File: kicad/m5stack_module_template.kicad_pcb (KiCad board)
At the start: 2 copper layers, 50 x 50 mm, 332 parts

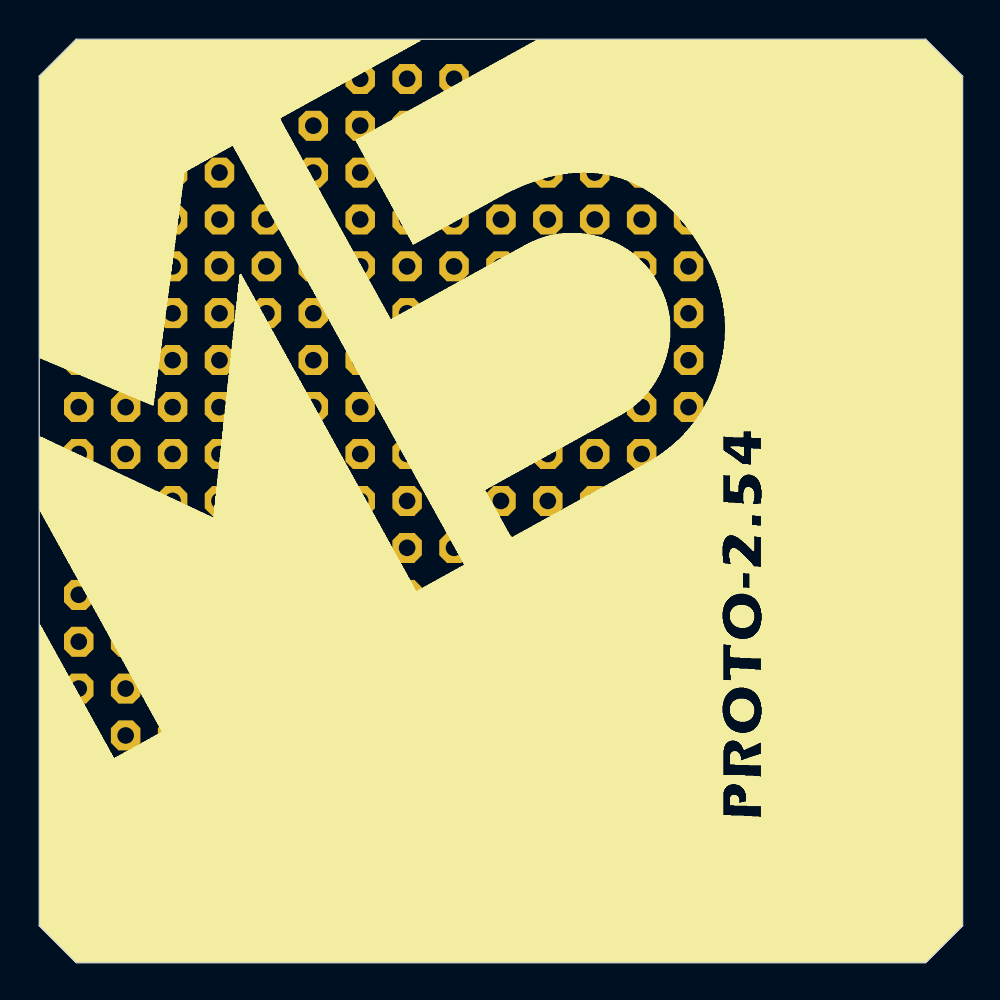
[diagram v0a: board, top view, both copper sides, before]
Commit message: Removed silkscreen and proto pads
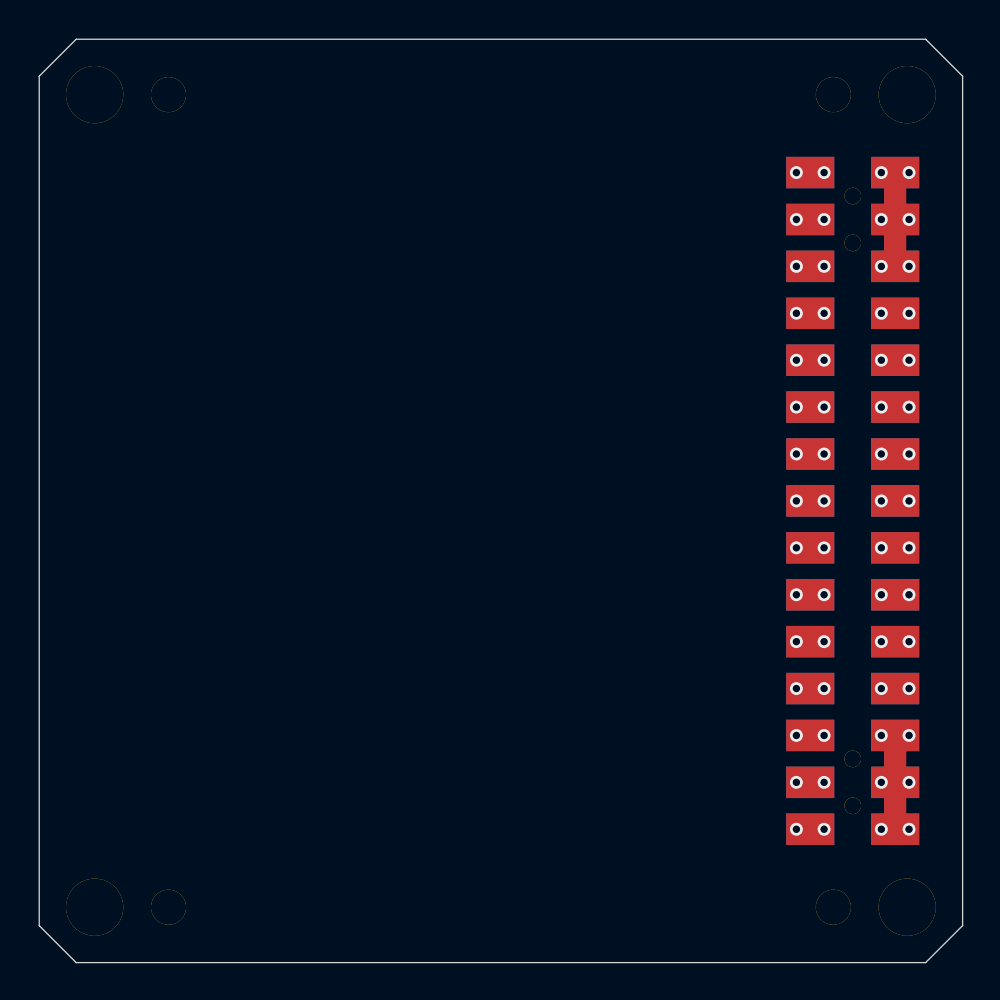
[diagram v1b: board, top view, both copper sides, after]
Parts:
- removed the ? at (26.9, 19.2)
- removed the ? at (49.7, 57.3)
- removed the ? at (37.0, 54.8)
- removed the ? at (34.5, 65.0)
- removed the ? at (34.5, 62.4)
- removed the ? at (34.5, 59.9)
- removed the ? at (34.5, 57.3)
- removed the ? at (34.5, 54.8)
- removed the ? at (31.9, 65.0)
- removed the ? at (31.9, 62.4)
- removed the ? at (31.9, 59.9)
- removed the ? at (31.9, 57.3)
- removed the ? at (52.3, 57.3)
- removed the ? at (31.9, 54.8)
- removed the ? at (29.4, 65.0)
- removed the ? at (29.4, 62.4)
- removed the ? at (29.4, 59.9)
- removed the ? at (29.4, 57.3)
- removed the ? at (29.4, 54.8)
- removed the ? at (26.9, 59.9)
- removed the ? at (26.9, 57.3)
- removed the ? at (26.9, 54.8)
- removed the ? at (26.9, 52.3)
- removed the ? at (52.3, 54.8)
- removed the ? at (26.9, 49.7)
- removed the ? at (26.9, 47.2)
- removed the ? at (26.9, 44.6)
- removed the ? at (26.9, 42.1)
- removed the ? at (24.3, 52.3)
- removed the ? at (24.3, 49.7)
- removed the ? at (24.3, 47.2)
- removed the ? at (24.3, 44.6)
- removed the ? at (24.3, 42.1)
- removed the ? at (21.8, 52.3)
- removed the ? at (37.0, 49.7)
- removed the ? at (21.8, 49.7)
- removed the ? at (21.8, 47.2)
- removed the ? at (21.8, 44.6)
- removed the ? at (21.8, 42.1)
- removed the ? at (19.2, 52.3)
- removed the ? at (19.2, 49.7)
- removed the ? at (19.2, 47.2)
- removed the ? at (19.2, 44.6)
- removed the ? at (19.2, 42.1)
- removed the ? at (19.2, 39.6)
- removed the ? at (37.0, 47.2)
- removed the ? at (21.8, 39.6)
- removed the ? at (24.3, 39.6)
- removed the ? at (26.9, 39.6)
- removed the ? at (19.2, 54.8)
- removed the ? at (21.8, 54.8)
- removed the ? at (24.3, 54.8)
- removed the ? at (19.2, 57.3)
- removed the ? at (21.8, 57.3)
- removed the ? at (24.3, 57.3)
- removed the ? at (19.2, 59.9)
- removed the ? at (37.0, 44.6)
- removed the ? at (21.8, 59.9)
- removed the ? at (24.3, 59.9)
- removed the ? at (47.2, 19.2)
- removed the ? at (49.7, 19.2)
- removed the ? at (52.3, 19.2)
- removed the ? at (39.6, 19.2)
- removed the ? at (42.1, 19.2)
- removed the ? at (44.6, 19.2)
- removed the ? at (31.9, 19.2)
- removed the ? at (34.5, 19.2)
- removed the ? at (37.0, 42.1)
- removed the ? at (37.0, 19.2)
- removed the ? at (47.2, 21.8)
- removed the ? at (49.7, 21.8)
- removed the ? at (52.3, 21.8)
- removed the ? at (39.6, 21.8)
- removed the ? at (42.1, 21.8)
- removed the ? at (44.6, 21.8)
- removed the ? at (31.9, 21.8)
- removed the ? at (34.5, 21.8)
- removed the ? at (37.0, 21.8)
- removed the ? at (37.0, 39.6)
- removed the ? at (29.4, 21.8)
- removed the ? at (29.4, 19.2)
- removed the ? at (29.4, 52.3)
- removed the ? at (31.9, 52.3)
- removed the ? at (34.5, 52.3)
- removed the ? at (37.0, 52.3)
- removed the ? at (29.4, 39.6)
- removed the ? at (29.4, 42.1)
- removed the ? at (29.4, 44.6)
- removed the ? at (29.4, 47.2)
- removed the ? at (34.5, 49.7)
- removed the ? at (29.4, 49.7)
- removed the ? at (49.7, 54.8)
- removed the ? at (29.4, 37.0)
- removed the ? at (26.9, 37.0)
- removed the ? at (24.3, 37.0)
- removed the ? at (21.8, 37.0)
- removed the ? at (19.2, 37.0)
- removed the ? at (47.2, 37.0)
- removed the ? at (44.6, 37.0)
- removed the ? at (42.1, 37.0)
- removed the ? at (34.5, 47.2)
- removed the ? at (39.6, 37.0)
- removed the ? at (31.9, 37.0)
- removed the ? at (34.5, 37.0)
- removed the ? at (37.0, 37.0)
- removed the ? at (37.0, 34.5)
- removed the ? at (34.5, 34.5)
- removed the ? at (31.9, 34.5)
- removed the ? at (39.6, 34.5)
- removed the ? at (42.1, 34.5)
- removed the ? at (44.6, 34.5)
- removed the ? at (34.5, 24.3)
- removed the ? at (34.5, 44.6)
- removed the ? at (47.2, 34.5)
- removed the ? at (19.2, 34.5)
- removed the ? at (21.8, 34.5)
- removed the ? at (24.3, 34.5)
- removed the ? at (26.9, 34.5)
- removed the ? at (29.4, 34.5)
- removed the ? at (49.7, 34.5)
- removed the ? at (52.3, 34.5)
- removed the ? at (37.0, 31.9)
- removed the ? at (34.5, 31.9)
- removed the ? at (34.5, 42.1)
- removed the ? at (31.9, 31.9)
- removed the ? at (39.6, 31.9)
- removed the ? at (42.1, 31.9)
- removed the ? at (44.6, 31.9)
- removed the ? at (47.2, 31.9)
- removed the ? at (19.2, 31.9)
- removed the ? at (21.8, 31.9)
- removed the ? at (24.3, 31.9)
- removed the ? at (26.9, 31.9)
- removed the ? at (29.4, 31.9)
- removed the ? at (34.5, 39.6)
- removed the ? at (49.7, 31.9)
- removed the ? at (52.3, 31.9)
- removed the ? at (37.0, 29.4)
- removed the ? at (34.5, 29.4)
- removed the ? at (31.9, 29.4)
- removed the ? at (39.6, 29.4)
- removed the ? at (42.1, 29.4)
- removed the ? at (44.6, 29.4)
- removed the ? at (47.2, 29.4)
- removed the ? at (19.2, 29.4)
- removed the ? at (31.9, 49.7)
- removed the ? at (21.8, 29.4)
- removed the ? at (24.3, 29.4)
- removed the ? at (26.9, 29.4)
- removed the ? at (29.4, 29.4)
- removed the ? at (49.7, 29.4)
- removed the ? at (52.3, 29.4)
- removed the ? at (37.0, 26.9)
- removed the ? at (34.5, 26.9)
- removed the ? at (31.9, 26.9)
- removed the ? at (39.6, 26.9)
- removed the ? at (31.9, 47.2)
- removed the ? at (42.1, 26.9)
- removed the ? at (44.6, 26.9)
- removed the ? at (47.2, 26.9)
- removed the ? at (19.2, 26.9)
- removed the ? at (21.8, 26.9)
- removed the ? at (24.3, 26.9)
- removed the ? at (26.9, 26.9)
- removed the ? at (29.4, 26.9)
- removed the ? at (49.7, 26.9)
- removed the ? at (52.3, 26.9)
- removed the ? at (31.9, 44.6)
- removed the ? at (37.0, 24.3)
- removed the ? at (31.9, 24.3)
- removed the ? at (39.6, 24.3)
- removed the ? at (42.1, 24.3)
- removed the ? at (44.6, 24.3)
- removed the ? at (47.2, 24.3)
- removed the ? at (19.2, 24.3)
- removed the ? at (21.8, 24.3)
- removed the ? at (24.3, 24.3)
- removed the ? at (26.9, 24.3)
- removed the ? at (31.9, 42.1)
- removed the ? at (29.4, 24.3)
- removed the ? at (49.7, 24.3)
- removed the ? at (52.3, 24.3)
- removed the ? at (49.7, 62.4)
- removed the ? at (52.3, 62.4)
- removed the ? at (49.7, 65.0)
- removed the ? at (52.3, 65.0)
- removed the ? at (54.8, 65.0)
- removed the ? at (54.8, 62.4)
- removed the ? at (54.8, 21.8)
- removed the ? at (31.9, 39.6)
- removed the ? at (57.3, 62.4)
- removed the ? at (57.3, 65.0)
- removed the ? at (57.3, 21.8)
- removed the ? at (52.3, 59.9)
- removed the ? at (42.1, 42.1)
- removed the ? at (49.7, 59.9)
- removed the ? at (44.6, 42.1)
- removed the ? at (47.2, 42.1)
- removed the ? at (49.7, 42.1)
- removed the ? at (52.3, 42.1)
- removed the ? at (39.6, 42.1)
- removed the ? at (39.6, 39.6)
- removed the ? at (42.1, 39.6)
- removed the ? at (44.6, 39.6)
- removed the ? at (47.2, 39.6)
- removed the ? at (52.3, 37.0)
- removed the ? at (49.7, 39.6)
- removed the ? at (52.3, 39.6)
- removed the ? at (52.3, 44.6)
- removed the ? at (49.7, 44.6)
- removed the ? at (47.2, 44.6)
- removed the ? at (44.6, 44.6)
- removed the ? at (42.1, 44.6)
- removed the ? at (39.6, 44.6)
- removed the ? at (39.6, 47.2)
- removed the ? at (52.3, 47.2)
- removed the ? at (49.7, 37.0)
- removed the ? at (49.7, 47.2)
- removed the ? at (47.2, 47.2)
- removed the ? at (44.6, 47.2)
- removed the ? at (42.1, 47.2)
- removed the ? at (52.3, 49.7)
- removed the ? at (49.7, 49.7)
- removed the ? at (47.2, 49.7)
- removed the ? at (44.6, 49.7)
- removed the ? at (42.1, 49.7)
- removed the ? at (39.6, 49.7)
- removed the ? at (26.9, 21.8)
- removed the ? at (39.6, 52.3)
- removed the ? at (52.3, 52.3)
- removed the ? at (49.7, 52.3)
- removed the ? at (47.2, 52.3)
- removed the ? at (44.6, 52.3)
- removed the ? at (42.1, 52.3)
- removed the ? at (47.2, 54.8)
- removed the ? at (44.6, 54.8)
- removed the ? at (42.1, 54.8)
- removed the ? at (39.6, 54.8)
- removed the ? at (26.9, 62.4)
- removed the ? at (39.6, 57.3)
- removed the ? at (47.2, 57.3)
- removed the ? at (44.6, 57.3)
- removed the ? at (42.1, 57.3)
- removed the ? at (47.2, 59.9)
- removed the ? at (44.6, 59.9)
- removed the ? at (42.1, 59.9)
- removed the ? at (39.6, 59.9)
- removed the ? at (39.6, 62.4)
- removed the ? at (47.2, 62.4)
- removed the ? at (26.9, 65.0)
- removed the ? at (44.6, 62.4)
- removed the ? at (42.1, 62.4)
- removed the ? at (42.1, 65.0)
- removed the ? at (44.6, 65.0)
- removed the ? at (47.2, 65.0)
- removed the ? at (39.6, 65.0)
- removed the ? at (37.0, 65.0)
- removed the ? at (37.0, 62.4)
- removed the ? at (37.0, 59.9)
- removed the ? at (37.0, 57.3)

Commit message: Create header footprint
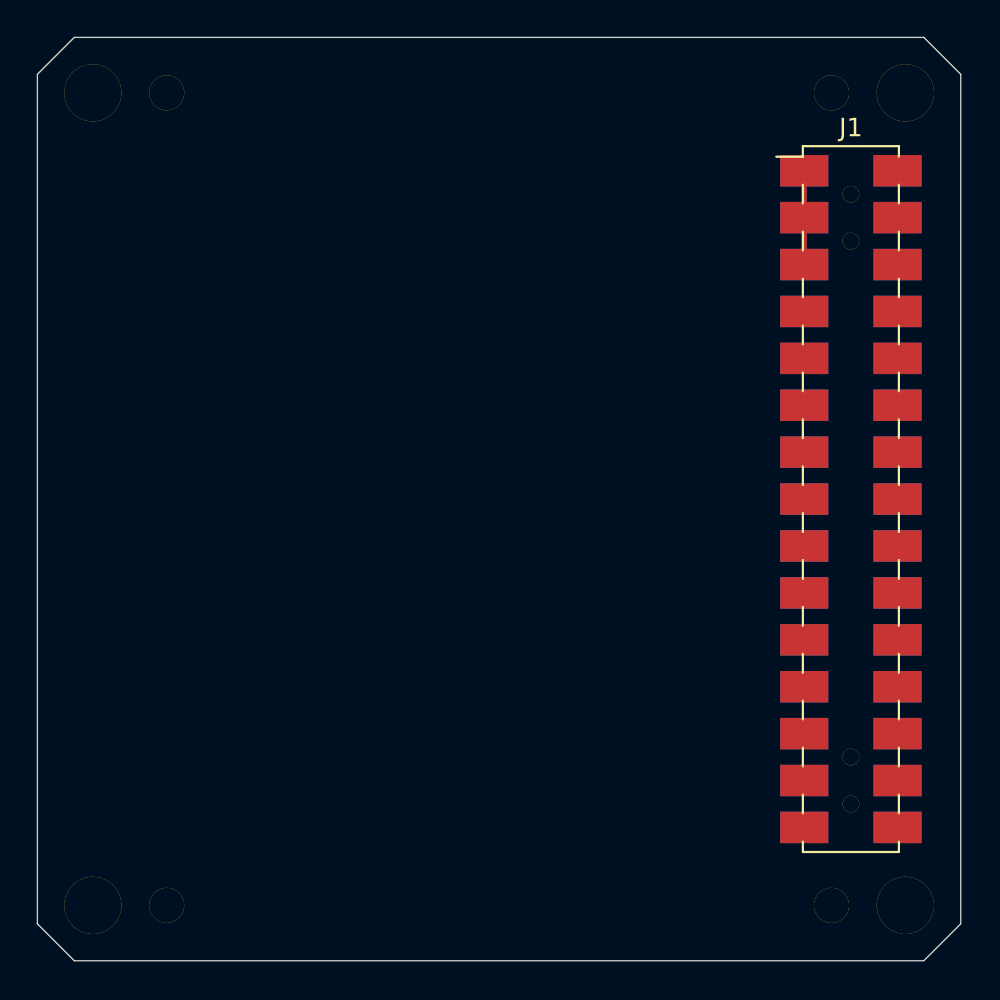
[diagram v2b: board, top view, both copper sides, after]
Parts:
- removed the ? at (58.9, 29.4) (x2)
- removed the ? at (63.5, 29.4) (x2)
- removed the ? at (63.5, 26.9) (x2)
- removed the ? at (58.9, 26.9) (x2)
- removed the ? at (63.5, 24.3) (x2)
- removed the ? at (58.9, 24.3) (x2)
- removed the ? at (58.9, 39.6) (x2)
- removed the ? at (63.5, 39.6) (x2)
- removed the ? at (63.5, 37.0) (x2)
- removed the ? at (58.9, 37.0) (x2)
- removed the ? at (63.5, 34.5) (x2)
- removed the ? at (58.9, 34.5) (x2)
- removed the ? at (63.5, 31.9) (x2)
- removed the ? at (58.9, 31.9) (x2)
- removed the ? at (58.9, 49.7) (x2)
- removed the ? at (63.5, 49.7) (x2)
- removed the ? at (63.5, 47.2) (x2)
- removed the ? at (58.9, 47.2) (x2)
- removed the ? at (63.5, 44.6) (x2)
- removed the ? at (58.9, 44.6) (x2)
- removed the ? at (63.5, 42.1) (x2)
- removed the ? at (58.9, 42.1) (x2)
- removed the ? at (58.9, 52.3) (x2)
- removed the ? at (63.5, 52.3) (x2)
- removed the ? at (58.9, 54.8) (x2)
- removed the ? at (63.5, 54.8) (x2)
- removed the ? at (58.9, 57.3) (x2)
- removed the ? at (63.5, 57.3) (x2)
- removed the ? at (63.5, 59.9) (x2)
- removed the ? at (58.9, 59.9) (x2)
- added J1: Conn_02x15_Odd_Even, M5Stack-Module-Template:M5Stack_PinHeader_2x15_P2.54mm, F.Cu at (61.1, 42.0)
- moved ? 0.14 mm to (64.0, 64.0)
- moved ? 0.14 mm to (20.0, 64.0)
- moved ? 0.14 mm to (64.0, 20.0)
- moved ? 0.14 mm to (24.0, 64.0)
- moved ? 0.14 mm to (61.1, 58.5)
- moved ? 0.14 mm to (61.1, 28.0)
- moved ? 0.14 mm to (61.1, 56.0)
- moved ? 0.14 mm to (20.0, 20.0)
- moved ? 0.14 mm to (24.0, 20.0)
- moved ? 0.14 mm to (60.0, 64.0)
- moved ? 0.14 mm to (61.1, 25.5)
- moved ? 0.14 mm to (60.0, 20.0)
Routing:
- net GND: track 0.00 -> 5.08 mm
- net (no net): vias 60 -> 0

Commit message: Reorganize footprint library
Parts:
- J1: footprint M5Stack-Module-Template:M5Stack_PinHeader_2x15_P2.54mm -> lib:M5Stack_PinHeader_2x15_P2.54mm
